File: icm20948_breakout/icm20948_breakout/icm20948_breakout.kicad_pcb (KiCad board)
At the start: 2 copper layers, 17.8 x 16.3 mm, 7 parts, among them J1 Conn_01x05_Male, J2 Conn_01x05_Male, U1 ICM-20948, U2 TPS7A0518PDBZR

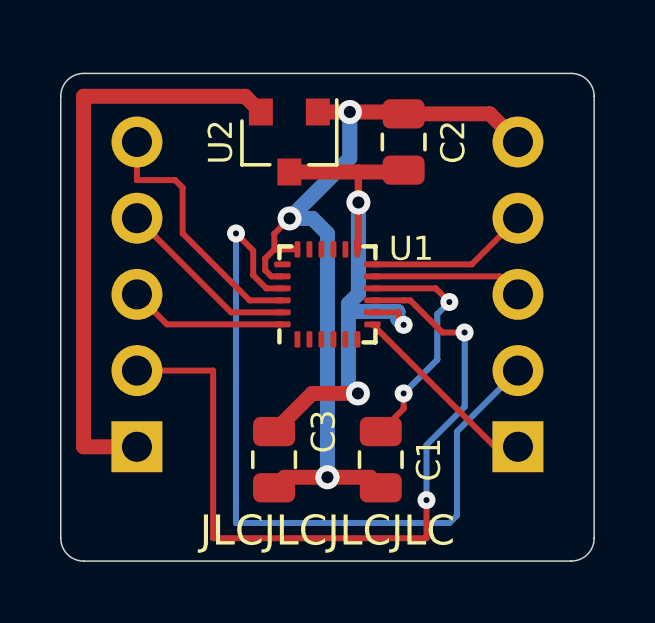
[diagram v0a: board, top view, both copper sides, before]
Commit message: Complete AD7147 breakout and create Cap Touch pad
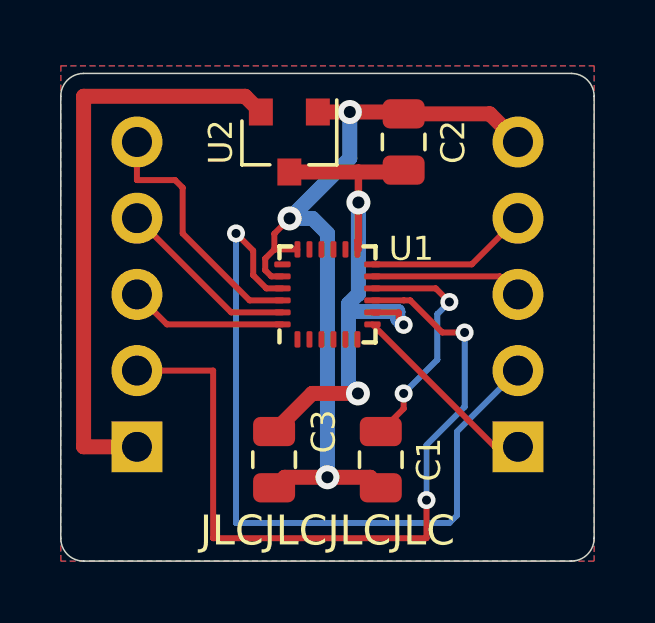
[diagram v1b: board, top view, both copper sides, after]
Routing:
- added copper zone on B.Cu, net GND
- added copper zone on F.Cu, net GND
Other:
- rule trace_min: 0.2 -> 0.15
- rule via_min_size: 0.2 -> 0.3

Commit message: Fix mixed up regulator pins on ICM20948 board
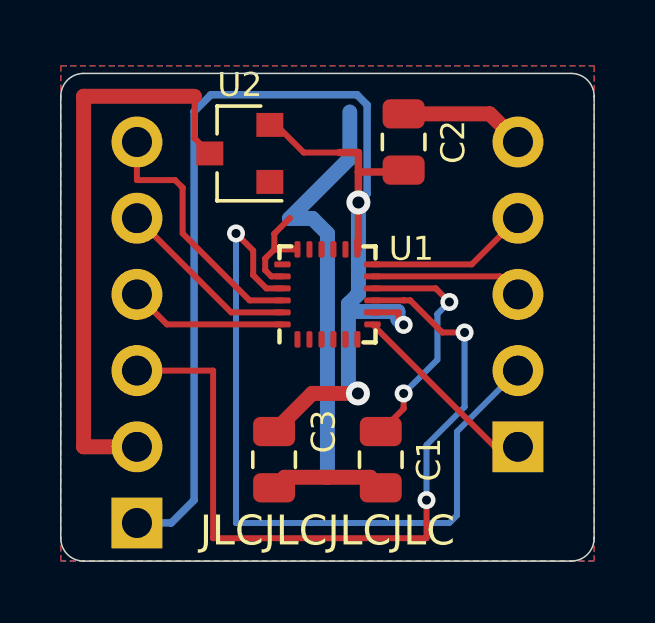
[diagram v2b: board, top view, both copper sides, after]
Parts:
- J1: value Conn_01x05_Male -> Conn_01x06_Male; footprint Connector_PinHeader_2.54mm:PinHeader_1x05_P2.54mm_Vertical -> Connector_PinHeader_2.54mm:PinHeader_1x06_P2.54mm_Vertical
- J2: value Conn_01x05_Male -> Conn_01x06_Male
- moved J1 2.54 mm to (139.7, 80.0)
- moved U2 1.69 mm to (143.1, 67.7), turned to 180 degrees
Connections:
- C2 pad 2: Net-(C2-Pad2) -> VOUT
- C3 pad 1: Net-(C2-Pad2) -> VOUT
- J1 pad 1: +3V3 -> VOUT
- J1 pad 2: Net-(J1-Pad2) -> VDD
- U1 pad 13: Net-(C2-Pad2) -> VOUT
- U1 pad 22: Net-(J1-Pad5) -> Net-(J1-Pad6)
- U1 pad 23: Net-(J1-Pad4) -> Net-(J1-Pad5)
- U1 pad 24: Net-(J1-Pad3) -> Net-(J1-Pad4)
- U1 pad 8: Net-(C2-Pad2) -> VOUT
- U1 pad 9: Net-(J1-Pad2) -> Net-(J1-Pad3)
- U2 pad 2: +3V3 -> VOUT
- U2 pad 3: Net-(C2-Pad2) -> VDD
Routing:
- net VOUT: track 0.00 -> 46.3 mm, vias 0 -> 3
- net Net-(J1-Pad2): track 26.1 -> 0.00 mm, vias 2 -> 0
- net Net-(J1-Pad3): track 5.26 -> 26.1 mm, vias 0 -> 2
- net Net-(C2-Pad2): track 19.9 -> 0.00 mm, vias 3 -> 0
- net +3V3: track 19.6 -> 0.00 mm
- net VDD: track 0.00 -> 19.3 mm
- net Net-(J1-Pad6): track 0.00 -> 9.18 mm
- net Net-(J1-Pad5): track 9.18 -> 6.15 mm
- net GND: track 29.1 -> 26.3 mm, vias 3 -> 0
- net Net-(J1-Pad4): track 6.15 -> 5.26 mm

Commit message: Reduce width of PCB, update pinout and silkscreen
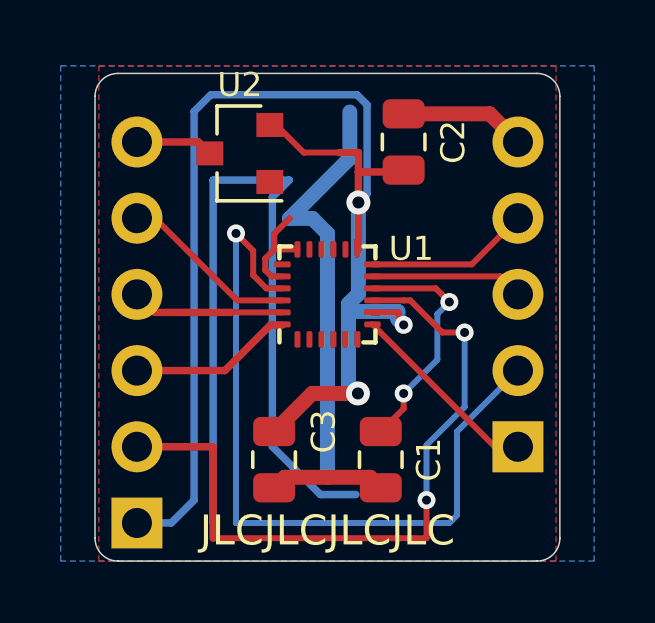
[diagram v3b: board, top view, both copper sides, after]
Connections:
- J1 pad 2: VDD -> Net-(J1-Pad2)
- J1 pad 6: Net-(J1-Pad6) -> VDD
- U1 pad 22: Net-(J1-Pad6) -> Net-(J1-Pad5)
- U1 pad 23: Net-(J1-Pad5) -> Net-(J1-Pad4)
- U1 pad 24: Net-(J1-Pad4) -> Net-(J1-Pad3)
- U1 pad 9: Net-(J1-Pad3) -> Net-(J1-Pad2)
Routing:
- net GND: track 26.3 -> 52.9 mm
- net Net-(J1-Pad2): track 0.00 -> 23.6 mm, vias 0 -> 2
- net Net-(J1-Pad3): track 26.1 -> 5.48 mm, vias 2 -> 0
- net VDD: track 19.3 -> 3.09 mm
- net Net-(J1-Pad6): track 9.18 -> 0.00 mm
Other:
- board size 17.8 x 16.3 mm -> 15.5 x 16.3 mm
- board text added: "ICM20948 B/O V0.02"
- board text added: "Vin 22 23 24 9 Vout"
- board text removed: "22 23 24 9 3.3"
- board text removed: "ICM20948 B/O V0.01"
